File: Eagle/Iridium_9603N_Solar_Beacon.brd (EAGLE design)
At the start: 33.3 x 36.2 mm, 55 parts, among them CON2 uFL, J1 SS4-10-3.50-X-D, Q1 DMG3415U-7, Q2 2N2222, Q3 DMG3415U-7, U1 MCP111T-240E/TT, U2 SPX3819-3.3, U3 LTC3225EDDB#TRMPBF, U4 AS179-92LF, U5 ATSAMD21G18_QFN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

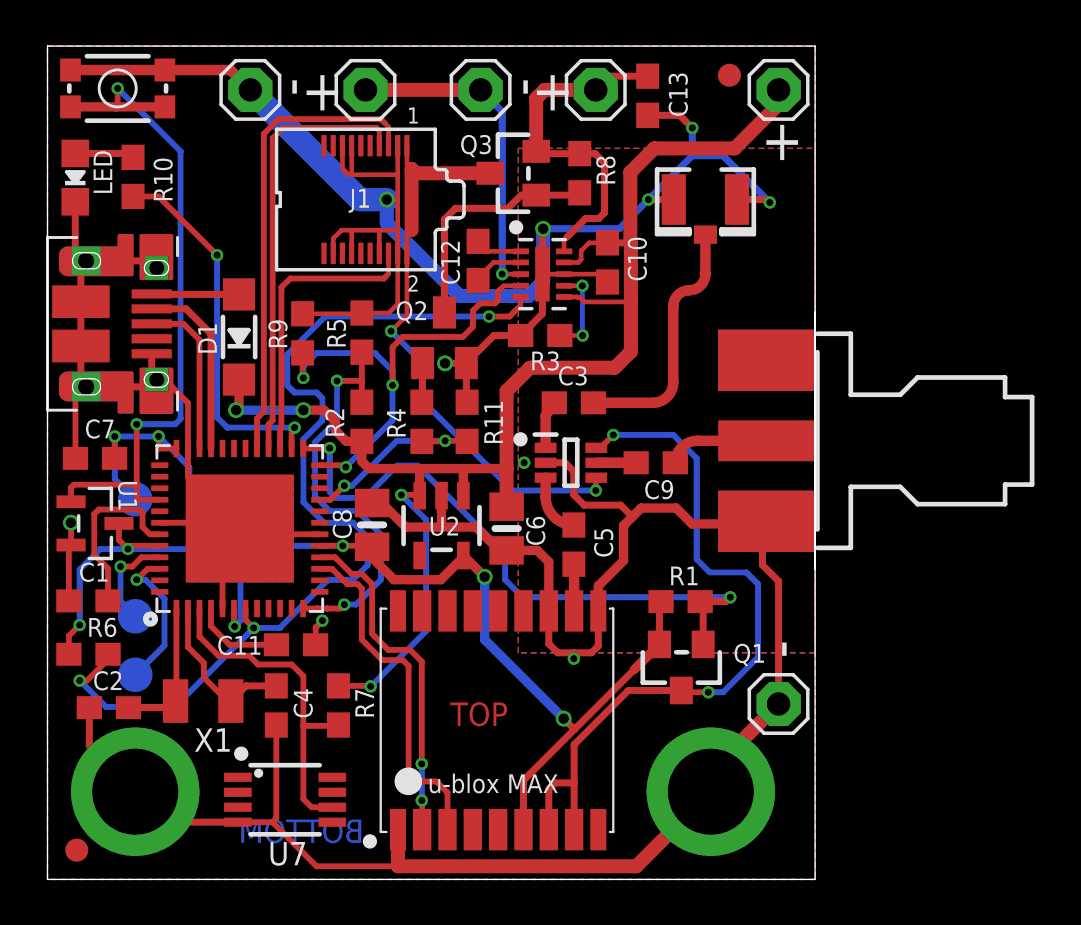
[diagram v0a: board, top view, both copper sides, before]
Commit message: Updated the PCB
Updated the PCB to improve the ground paths around the SAMD; added extra decoupling capacitors. Minor updates to the Arduino code.
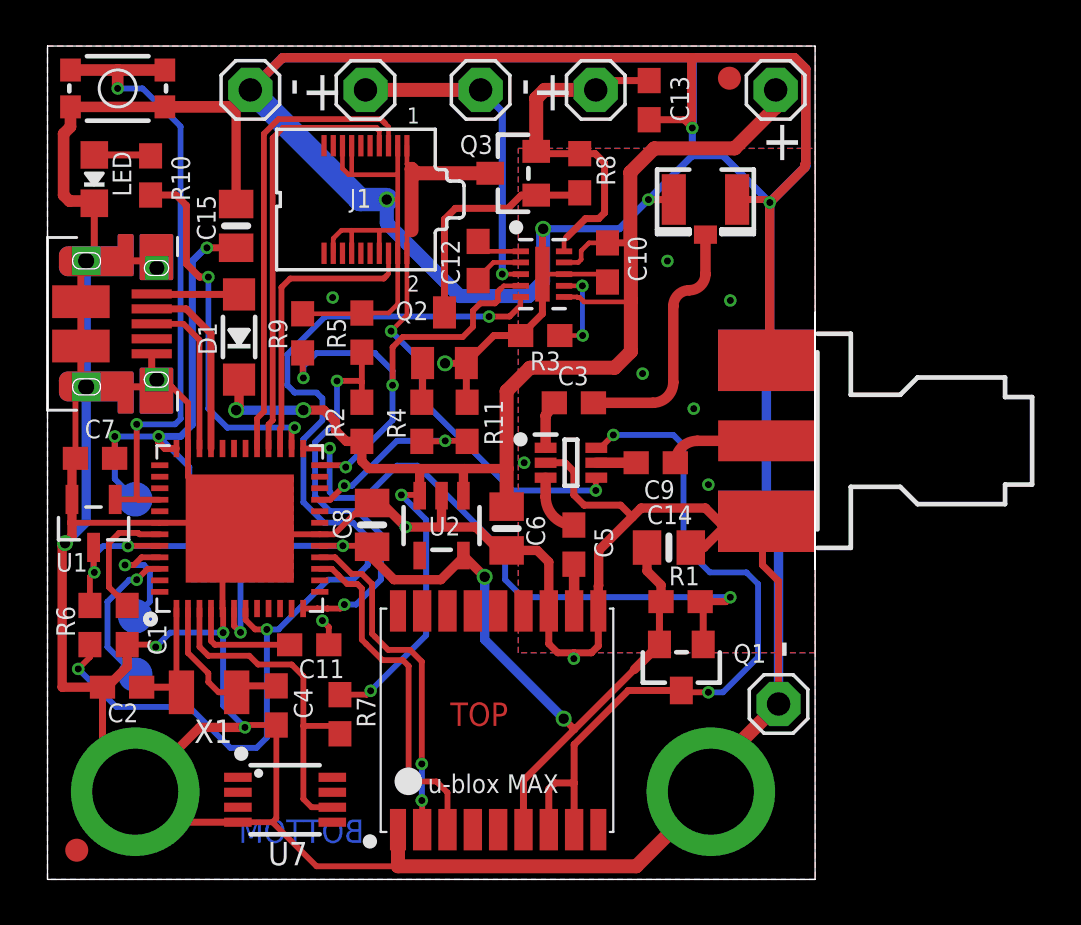
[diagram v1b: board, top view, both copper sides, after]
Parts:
- added C14, C15: 10µF, microbuilder:0805-NO
- moved C1 1.98 mm to (3.46, 11.0), turned to 270 degrees
- moved R6 1.27 mm to (1.84, 11.0), turned to 270 degrees
- moved C2 1.06 mm to (3.24, 8.35)
- moved LED 0.83 mm to (2.03, 30.4)
- moved R10 0.76 mm to (4.48, 30.6)
- moved C11 0.57 mm to (11.4, 10.2)
- moved X1 0.46 mm to (7.02, 8.13)
- moved R7 0.39 mm to (12.7, 7.18)
- moved C13 0.20 mm to (26.1, 33.8)
- moved SOLAR+ 0.13 mm to (31.6, 34.3)
- moved FD2 0.13 mm to (29.6, 34.8)
- moved U1 0.06 mm to (2.00, 15.5), turned to 180 degrees
- turned SW1 to 180 degrees
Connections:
- net +3V3: now also C14.1, C15.1
- net GND: now also C14.2, C15.2
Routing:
- net GND: track 209.9 -> 367.3 mm, vias 10 -> 20
- net +3V3: track 66.5 -> 77.7 mm, vias 8 -> 9
- net A1: track 42.3 -> 46.9 mm
- net VDDCORE1: track 7.76 -> 5.45 mm
- net !RESET: track 30.2 -> 28.3 mm
- net AREF: track 3.95 -> 4.89 mm
- net SWCLK: track 4.29 -> 5.07 mm
- net N$5: track 6.20 -> 5.55 mm

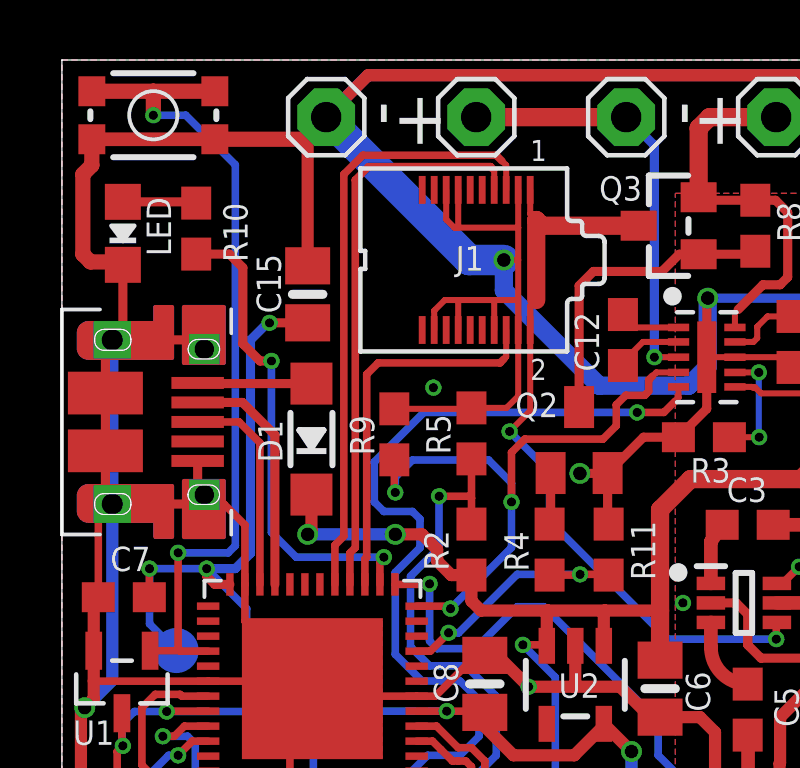
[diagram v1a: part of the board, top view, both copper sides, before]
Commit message: Connected the Ring Indicator
Connected the 9603N Ring Indicator to D21 just in case the solar beacon is used as a very compact Beacon Base (powered by USB).
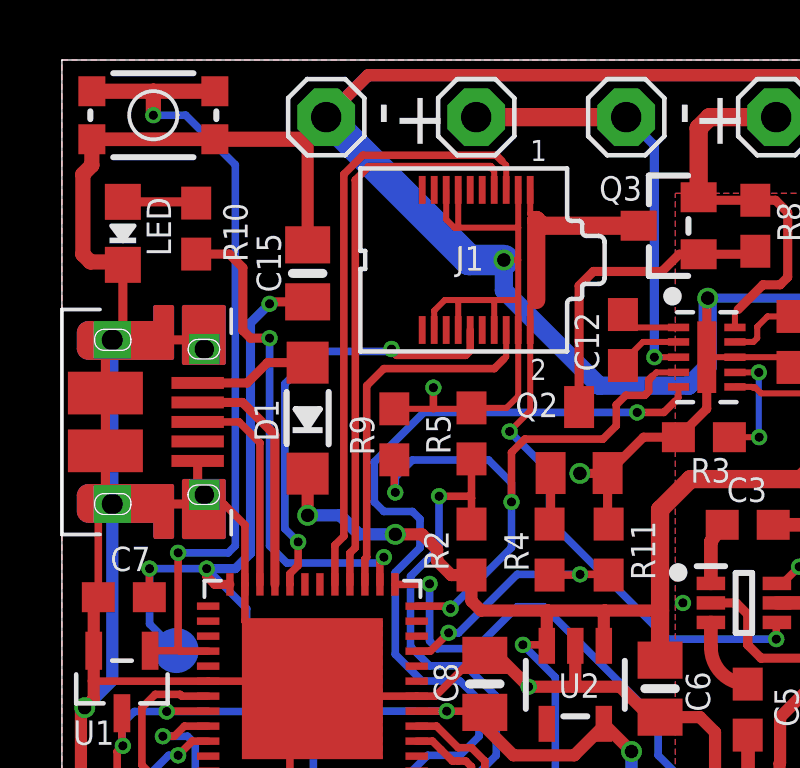
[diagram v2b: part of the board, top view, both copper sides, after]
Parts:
- moved D1 0.71 mm to (8.19, 24.3)
- moved C15 0.70 mm to (8.19, 29.1)
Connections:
- net SCL: now also J1.12
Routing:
- net SCL: track 0.00 -> 14.5 mm, vias 0 -> 2
- net +3V3: track 77.7 -> 78.3 mm
- net D13: track 16.2 -> 16.8 mm
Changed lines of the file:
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@@
 <attribute name="NAME" x="6.19125" y="29.464" size="0.8128" layer="25" font="vector" ratio="18" rot="R90"/>
 </element>
-<element name="D1" library="microbuilder" package="SOD-123" value="MBR120" x="8.3185" y="23.5585" smashed="yes" rot="R90">
-<attribute name="NAME" x="6.5405" y="24.1935" size="0.8128" layer="25" ratio="18" rot="R270"/>
+<element name="D1" library="microbuilder" package="SOD-123" value="MBR120" x="8.1915" y="24.257" smashed="yes" rot="R90">
+<attribute name="NAME" x="6.4135" y="24.892" size="0.8128" layer="25" ratio="18" rot="R270"/>
 </element>
 <element name="SOLAR-" library="adafruit" package="1X01" value="" x="31.75" y="7.62" smashed="yes">
@@
 <attribute name="NAME" x="26.035" y="15.4305" size="0.8128" layer="25" ratio="18"/>
 </element>
-<element name="C15" library="microbuilder" package="0805-NO" value="10µF" x="8.1915" y="28.3845" smashed="yes" rot="R90">
-<attribute name="NAME" x="7.3025" y="27.7495" size="0.8128" layer="25" ratio="18" rot="R90"/>
+<element name="C15" library="microbuilder" package="0805-NO" value="10µF" x="8.1915" y="29.083" smashed="yes" rot="R90">
+<attribute name="NAME" x="7.3025" y="28.448" size="0.8128" layer="25" ratio="18" rot="R90"/>
 </element>
 </elements>
@@
 <wire x1="18.06325" y1="16.6671" x2="18.06325" y2="17.80925" width="0.4064" layer="1"/>
 <wire x1="18.06325" y1="17.80925" x2="18.0975" y2="17.8435" width="0.4064" layer="1"/>
-<wire x1="8.3185" y1="21.7085" x2="8.3185" y2="20.5105" width="0.4064" layer="1"/>
-<wire x1="8.3185" y1="20.5105" x2="8.1915" y2="20.3835" width="0.4064" layer="1"/>
-<via x="8.1915" y="20.3835" extent="1-16" drill="0.45"/>
-<wire x1="8.1915" y1="20.3835" x2="11.1125" y2="20.3835" width="0.4064" layer="16"/>
+<wire x1="8.1915" y1="22.407" x2="8.1915" y2="21.0185" width="0.4064" layer="1"/>
+<via x="8.1915" y="21.0185" extent="1-16" drill="0.45"/>
+<wire x1="9.906" y1="20.3835" x2="11.1125" y2="20.3835" width="0.4064" layer="16"/>
+<wire x1="9.906" y1="20.3835" x2="9.271" y2="21.0185" width="0.4064" layer="16"/>
+<wire x1="9.271" y1="21.0185" x2="8.1915" y2="21.0185" width="0.4064" layer="16"/>
 <via x="11.1125" y="20.3835" extent="1-16" drill="0.45"/>
 <wire x1="11.1125" y1="20.3835" x2="12.0015" y2="20.3835" width="0.4064" layer="1"/>
@@
 <wire x1="14.82" y1="24.599" x2="13.6525" y2="24.599" width="0.2032" layer="1"/>
 <wire x1="15.20998125" y1="24.98898125" x2="14.82" y2="24.599" width="0.2032" layer="1"/>
-<wire x1="13.62075" y1="24.56725" x2="11.08075" y2="24.56725" width="0.2032" layer="1"/>
+<wire x1="13.62075" y1="24.56725" x2="12.3825" y2="24.56725" width="0.2032" layer="1"/>
+<wire x1="12.3825" y1="24.56725" x2="11.08075" y2="24.56725" width="0.2032" layer="1"/>
 <wire x1="6.10025" y1="18.715" x2="6.10025" y2="20.69675" width="0.254" layer="1"/>
 <wire x1="5.40258125" y1="21.39441875" x2="4.437378125" y2="21.39441875" width="0.254" layer="1"/>
@@
 <wire x1="28.5026" y1="14.4145" x2="29.5275" y2="15.4394" width="0.4064" layer="1"/>
 <contactref element="C15" pad="2"/>
-<wire x1="8.1915" y1="29.3345" x2="8.1915" y2="33.435490625" width="0.4064" layer="1"/>
+<wire x1="8.1915" y1="30.033" x2="8.1915" y2="33.435490625" width="0.4064" layer="1"/>
 <wire x1="8.1915" y1="33.435490625" x2="8.073490625" y2="33.5535" width="0.4064" layer="1"/>
 <wire x1="8.809990625" y1="34.29" x2="10.206990625" y2="35.687" width="0.4064" layer="1"/>
@@
 <wire x1="32.9343" y1="35.2012" x2="32.9343" y2="30.9658" width="0.4064" layer="16"/>
 <wire x1="28.0035" y1="32.639" x2="28.0035" y2="35.687" width="0.4064" layer="16"/>
+<wire x1="12.3825" y1="25.273" x2="12.3825" y2="24.56725" width="0.254" layer="1"/>
 </signal>
 <signal name="MOSI">
@@
 <contactref element="C15" pad="1"/>
 <wire x1="4.826" y1="19.2405" x2="5.7785" y2="19.2405" width="0.3048" layer="16"/>
-<wire x1="6.2865" y1="19.7485" x2="6.2865" y2="26.8605" width="0.3048" layer="16"/>
-<wire x1="6.9215" y1="27.432" x2="6.858" y2="27.432" width="0.3048" layer="16"/>
-<wire x1="6.858" y1="27.432" x2="6.2865" y2="26.8605" width="0.3048" layer="16"/>
-<via x="6.9215" y="27.432" extent="1-16" drill="0.3"/>
-<wire x1="6.9215" y1="27.432" x2="6.924" y2="27.4345" width="0.3048" layer="1"/>
-<wire x1="6.924" y1="27.4345" x2="8.1915" y2="27.4345" width="0.3048" layer="1"/>
+<wire x1="6.2865" y1="19.7485" x2="6.2865" y2="27.432" width="0.3048" layer="16"/>
+<wire x1="6.9215" y1="28.067" x2="6.2865" y2="27.432" width="0.3048" layer="16"/>
+<via x="6.9215" y="28.067" extent="1-16" drill="0.3"/>
+<wire x1="6.9215" y1="28.067" x2="6.9875" y2="28.133" width="0.3048" layer="1"/>
+<wire x1="6.9875" y1="28.133" x2="8.1915" y2="28.133" width="0.3048" layer="1"/>
 <wire x1="5.7785" y1="19.2405" x2="6.2865" y2="19.7485" width="0.3048" layer="16"/>
 <wire x1="5.60025" y1="18.715" x2="5.0975" y2="18.715" width="0.3048" layer="1"/>
@@
 <wire x1="10.60025" y1="19.49025" x2="10.7315" y2="19.6215" width="0.254" layer="1"/>
 <via x="10.7315" y="19.6215" extent="1-16" drill="0.3"/>
-<wire x1="10.7315" y1="19.6215" x2="7.8105" y2="19.6215" width="0.254" layer="16"/>
-<wire x1="6.985" y1="20.447" x2="7.8105" y2="19.6215" width="0.254" layer="16"/>
-<via x="6.985" y="26.162" extent="1-16" drill="0.3"/>
-<wire x1="6.985" y1="26.162" x2="6.985" y2="20.447" width="0.254" layer="16"/>
-<wire x1="6.985" y1="26.162" x2="6.604" y2="26.162" width="0.3048" layer="1"/>
+<wire x1="10.7315" y1="19.6215" x2="10.541" y2="19.431" width="0.254" layer="16"/>
+<wire x1="10.541" y1="19.431" x2="7.493" y2="19.431" width="0.254" layer="16"/>
+<wire x1="6.9215" y1="20.0025" x2="7.493" y2="19.431" width="0.254" layer="16"/>
+<via x="6.9215" y="26.924" extent="1-16" drill="0.3"/>
+<wire x1="6.9215" y1="26.924" x2="6.9215" y2="20.0025" width="0.254" layer="16"/>
 <wire x1="5.58075" y1="29.72525" x2="4.47675" y2="29.72525" width="0.3048" layer="1"/>
-<wire x1="6.604" y1="26.162" x2="6.0325" y2="26.7335" width="0.3048" layer="1"/>
-<wire x1="6.0325" y1="26.7335" x2="6.0325" y2="29.2735" width="0.3048" layer="1"/>
+<wire x1="6.9215" y1="26.924" x2="6.2865" y2="26.924" width="0.3048" layer="1"/>
+<wire x1="6.2865" y1="26.924" x2="6.0325" y2="27.178" width="0.3048" layer="1"/>
+<wire x1="6.0325" y1="27.178" x2="6.0325" y2="29.2735" width="0.3048" layer="1"/>
 <wire x1="6.0325" y1="29.2735" x2="5.58075" y2="29.72525" width="0.3048" layer="1"/>
 </signal>
@@
 <signal name="SCL">
 <contactref element="U5" pad="32"/>
+<contactref element="J1" pad="12"/>
+<via x="7.874" y="20.1295" extent="1-16" drill="0.3"/>
+<wire x1="7.59625" y1="19.06738125" x2="7.59625" y2="18.719" width="0.254" layer="1"/>
+<wire x1="7.60025" y1="18.715" x2="7.59625" y2="18.719" width="0.254" layer="1"/>
+<wire x1="7.874" y1="19.34513125" x2="7.874" y2="20.1295" width="0.254" layer="1"/>
+<wire x1="7.59625" y1="19.06738125" x2="7.874" y2="19.34513125" width="0.254" layer="1"/>
+<wire x1="7.874" y1="20.1295" x2="7.4295" y2="20.574" width="0.254" layer="16"/>
+<wire x1="7.4295" y1="25.4" x2="8.509" y2="26.4795" width="0.254" layer="16"/>
+<wire x1="8.509" y1="26.4795" x2="10.903" y2="26.4795" width="0.254" layer="16"/>
+<wire x1="10.903" y1="26.4795" x2="10.9855" y2="26.562" width="0.254" layer="16"/>
+<via x="10.9855" y="26.562" extent="1-16" drill="0.3"/>
+<wire x1="11.15614375" y1="26.3505" x2="10.9855" y2="26.52114375" width="0.254" layer="1"/>
+<wire x1="10.9855" y1="26.562" x2="10.9855" y2="26.52114375" width="0.254" layer="1"/>
+<wire x1="13.60998125" y1="26.50048125" x2="13.60998125" y2="27.195040625" width="0.254" layer="1"/>
+<wire x1="7.4295" y1="20.574" x2="7.4295" y2="25.4" width="0.254" layer="16"/>
+<wire x1="11.15614375" y1="26.3505" x2="13.46" y2="26.3505" width="0.254" layer="1"/>
+<wire x1="13.46" y1="26.3505" x2="13.60998125" y2="26.50048125" width="0.254" layer="1"/>
 </signal>
 <signal name="SDA">
@@
 <wire x1="10.10025" y1="18.715" x2="10.10025" y2="19.56175" width="0.254" layer="1"/>
 <wire x1="10.10025" y1="19.56175" x2="10.16" y2="19.6215" width="0.254" layer="1"/>
-<wire x1="14.605" y1="26.0985" x2="14.732" y2="26.2255" width="0.254" layer="1"/>
+<wire x1="14.4145" y1="25.908" x2="14.732" y2="26.2255" width="0.254" layer="1"/>
 <wire x1="14.732" y1="26.2255" x2="14.80998125" y2="26.30348125" width="0.2032" layer="1"/>
 <wire x1="14.80998125" y1="26.30348125" x2="14.80998125" y2="27.195040625" width="0.2032" layer="1"/>
-<wire x1="10.16" y1="19.6215" x2="10.16" y2="25.7175" width="0.254" layer="1"/>
-<wire x1="10.16" y1="25.7175" x2="10.541" y2="26.0985" width="0.254" layer="1"/>
-<wire x1="10.541" y1="26.0985" x2="14.605" y2="26.0985" width="0.254" layer="1"/>
+<wire x1="10.16" y1="19.6215" x2="10.16" y2="25.3365" width="0.254" layer="1"/>
+<wire x1="10.16" y1="25.3365" x2="10.7315" y2="25.908" width="0.254" layer="1"/>
+<wire x1="10.7315" y1="25.908" x2="14.4145" y2="25.908" width="0.254" layer="1"/>
 </signal>
 <signal name="D+">
@@
 <contactref element="CON1" pad="VBUS"/>
 <contactref element="D1" pad="A"/>
-<wire x1="4.525" y1="25.43" x2="4.5465" y2="25.4085" width="0.3048" layer="1"/>
-<wire x1="4.5465" y1="25.4085" x2="8.3185" y2="25.4085" width="0.3048" layer="1"/>
+<wire x1="8.1915" y1="26.107" x2="6.853" y2="26.107" width="0.3048" layer="1"/>
+<wire x1="6.853" y1="26.107" x2="6.176" y2="25.43" width="0.3048" layer="1"/>
+<wire x1="4.525" y1="25.43" x2="6.176" y2="25.43" width="0.3048" layer="1"/>
 </signal>
 <signal name="N$11">

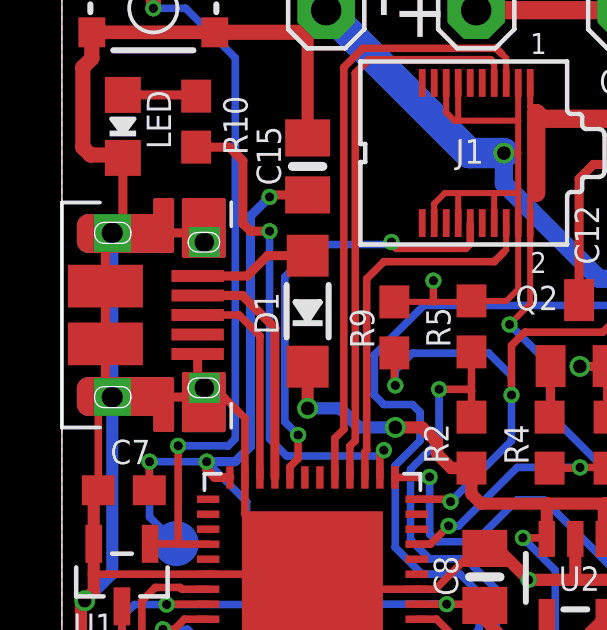
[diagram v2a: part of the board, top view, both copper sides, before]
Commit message: Corrected the zero width polygons
Corrected the zero width polygons in the micro USB connector that would have caused problems for OSH Park. Thanks go to Paul Loewen @ usask.ca
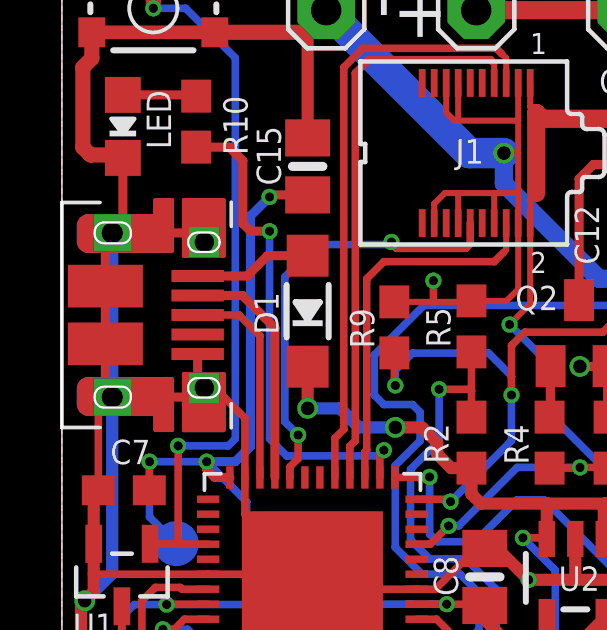
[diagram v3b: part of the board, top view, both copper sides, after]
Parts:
- CON1: device microbuilder:FCI_10103594 -> Iridium_9603_Beacon:MICROBUILDER_FCI_10103594_CORRECTED
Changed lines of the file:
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@@
 <layer number="59" name="tCarbon" color="7" fill="1" visible="no" active="no"/>
 <layer number="60" name="bCarbon" color="7" fill="1" visible="no" active="no"/>
+<layer number="88" name="SimResults" color="9" fill="1" visible="no" active="no"/>
+<layer number="89" name="SimProbes" color="9" fill="1" visible="no" active="no"/>
 <layer number="90" name="Modules" color="5" fill="1" visible="no" active="no"/>
 <layer number="91" name="Nets" color="2" fill="1" visible="no" active="no"/>
@@
 <attribute name="VALUE" x="5.588" y="35.8775" size="0.8128" layer="27" rot="R180" align="top-left"/>
 </element>
-<element name="CON1" library="microbuilder" package="FCI_10103594" value="" x="0" y="24.13" smashed="yes" rot="R270">
+<element name="CON1" library="Iridium_9603_Beacon" package="MICROBUILDER_FCI_10103594_CORRECTED" value="" x="0" y="24.13" smashed="yes" rot="R270">
 <attribute name="VALUE" x="-1.9523" y="27.924" size="0.4064" layer="27" ratio="10" rot="R270"/>
 </element>
